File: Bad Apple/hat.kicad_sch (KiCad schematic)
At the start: 6 parts, among them J1 GPIO, U1 CAT24C256

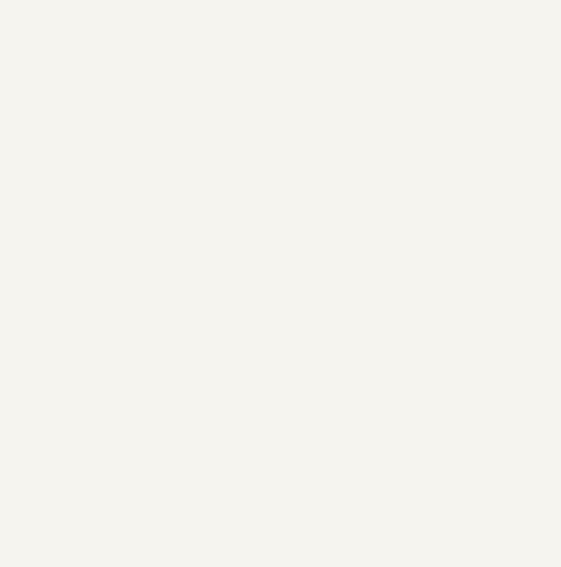
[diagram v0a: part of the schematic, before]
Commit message: chore(pcb): metadata stuff
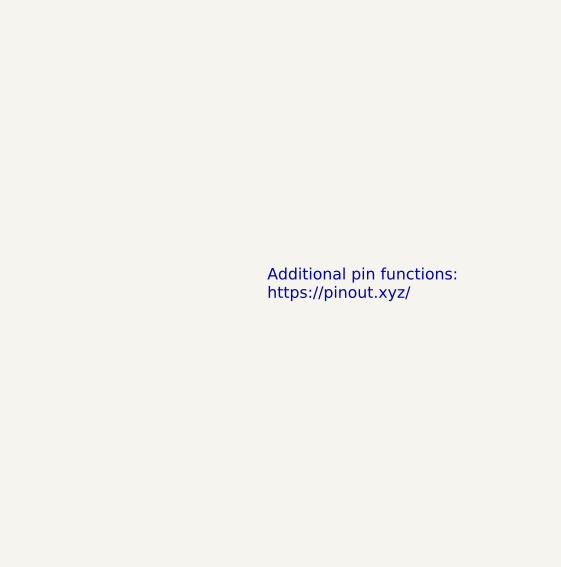
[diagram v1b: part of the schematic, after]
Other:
- note added: "Additional pin functions: https://pinout.xyz/"
- company: (none) -> Mixed Engineering Group 3 | STEM 12-Altruism / AY 2526 | CIT-U SHS
- title: (none) -> Autonomous  Courier Robot "Bad Apple"
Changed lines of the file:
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@@
 	(generator_version "9.0")
 	(paper "A4")
+	(title_block
+		(title "Autonomous  Courier Robot \"Bad Apple\"")
+		(date "2025-08-28")
+		(rev "1")
+		(company "Mixed Engineering Group 3 | STEM 12-Altruism / AY 2526 | CIT-U SHS")
+		(comment 4 "This sheet defines the Raspberry Pi HAT interface")
+	)
 	(text "ID_SD and ID_SC PINS:\nThese pins are reserved for HAT ID EEPROM.\n\nAt boot time this I2C interface will be\ninterrogated to look for an EEPROM\nthat identifes the attached board and\nallows automagic setup of the GPIOs\n(and optionally, Linux drivers).\n\nBridging JP1 enables write protection.\n\nDO NOT USE these pins for anything other\nthan attaching an I2C ID EEPROM. Leave\nunconnected if ID EEPROM not required."
 		(exclude_from_sim no)
@@
 		(effects
 			(font
+				(size 1.27 1.27)
+			)
+			(justify left bottom)
+		)
+	)
+	(text "Additional pin functions:\nhttps://pinout.xyz/"
+		(exclude_from_sim no)
+		(at 176.53 165.1 0)
+		(effects
+			(font

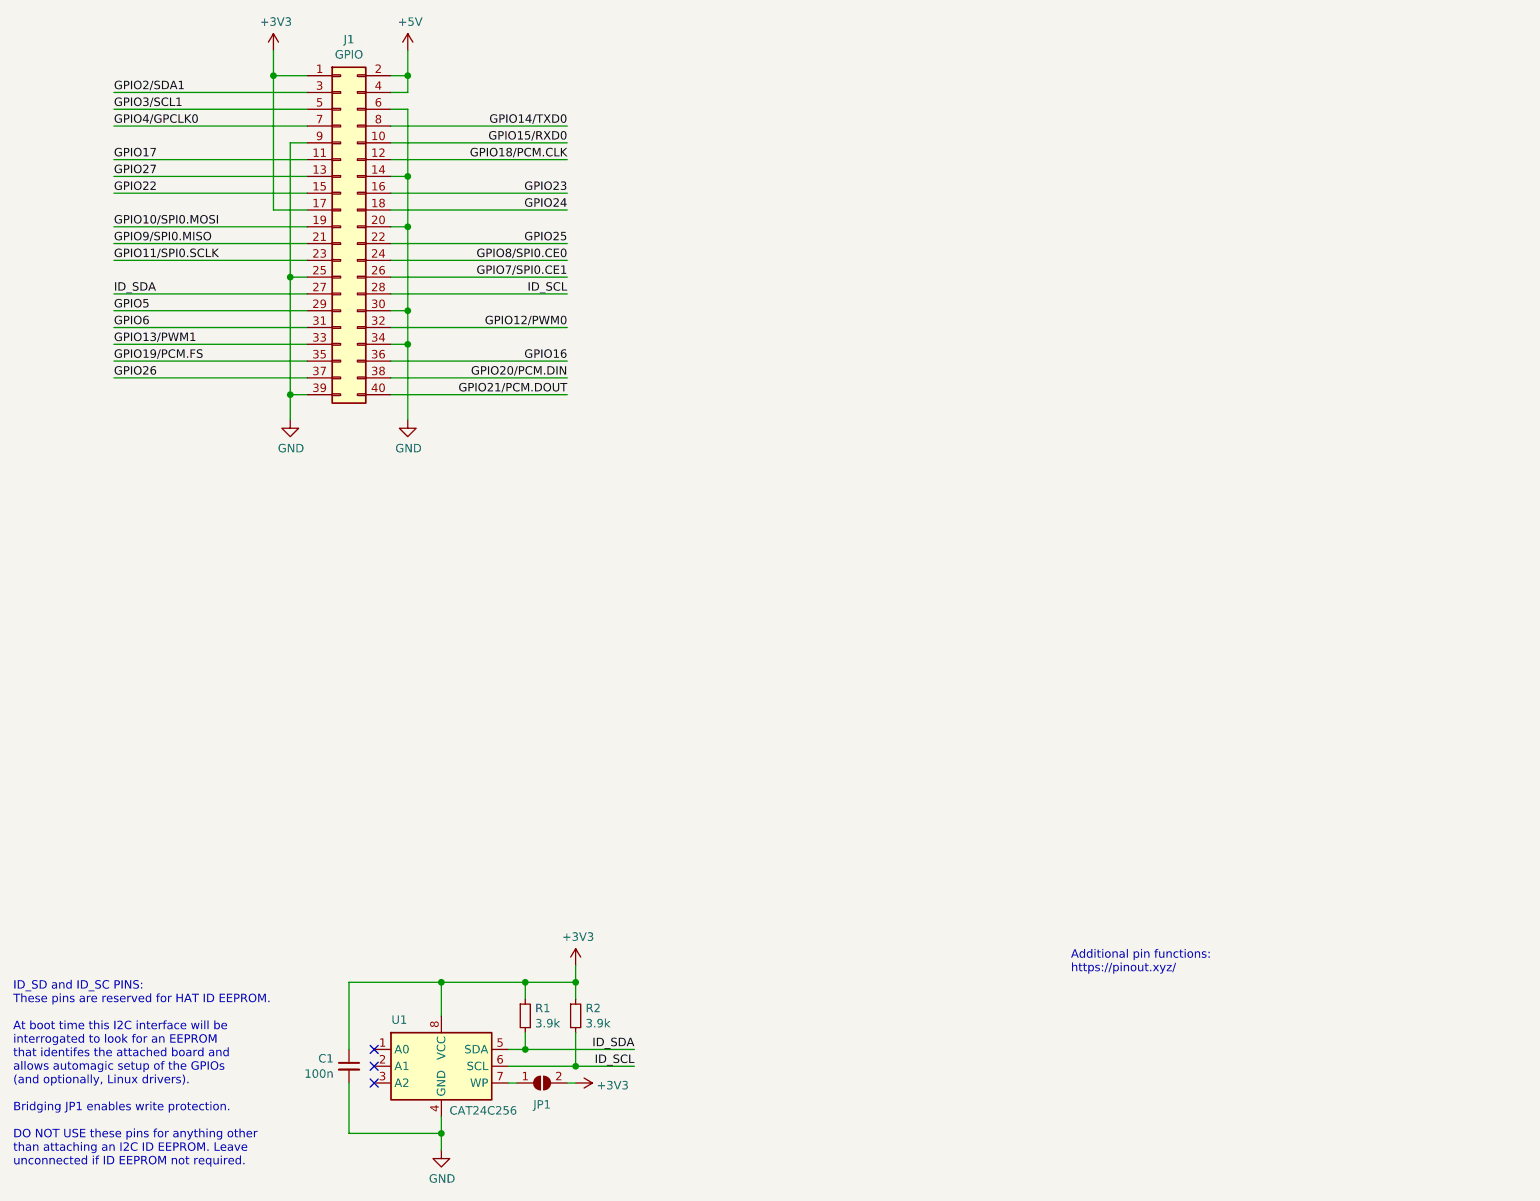
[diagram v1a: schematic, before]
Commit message: feat(pcb): motor subsystem
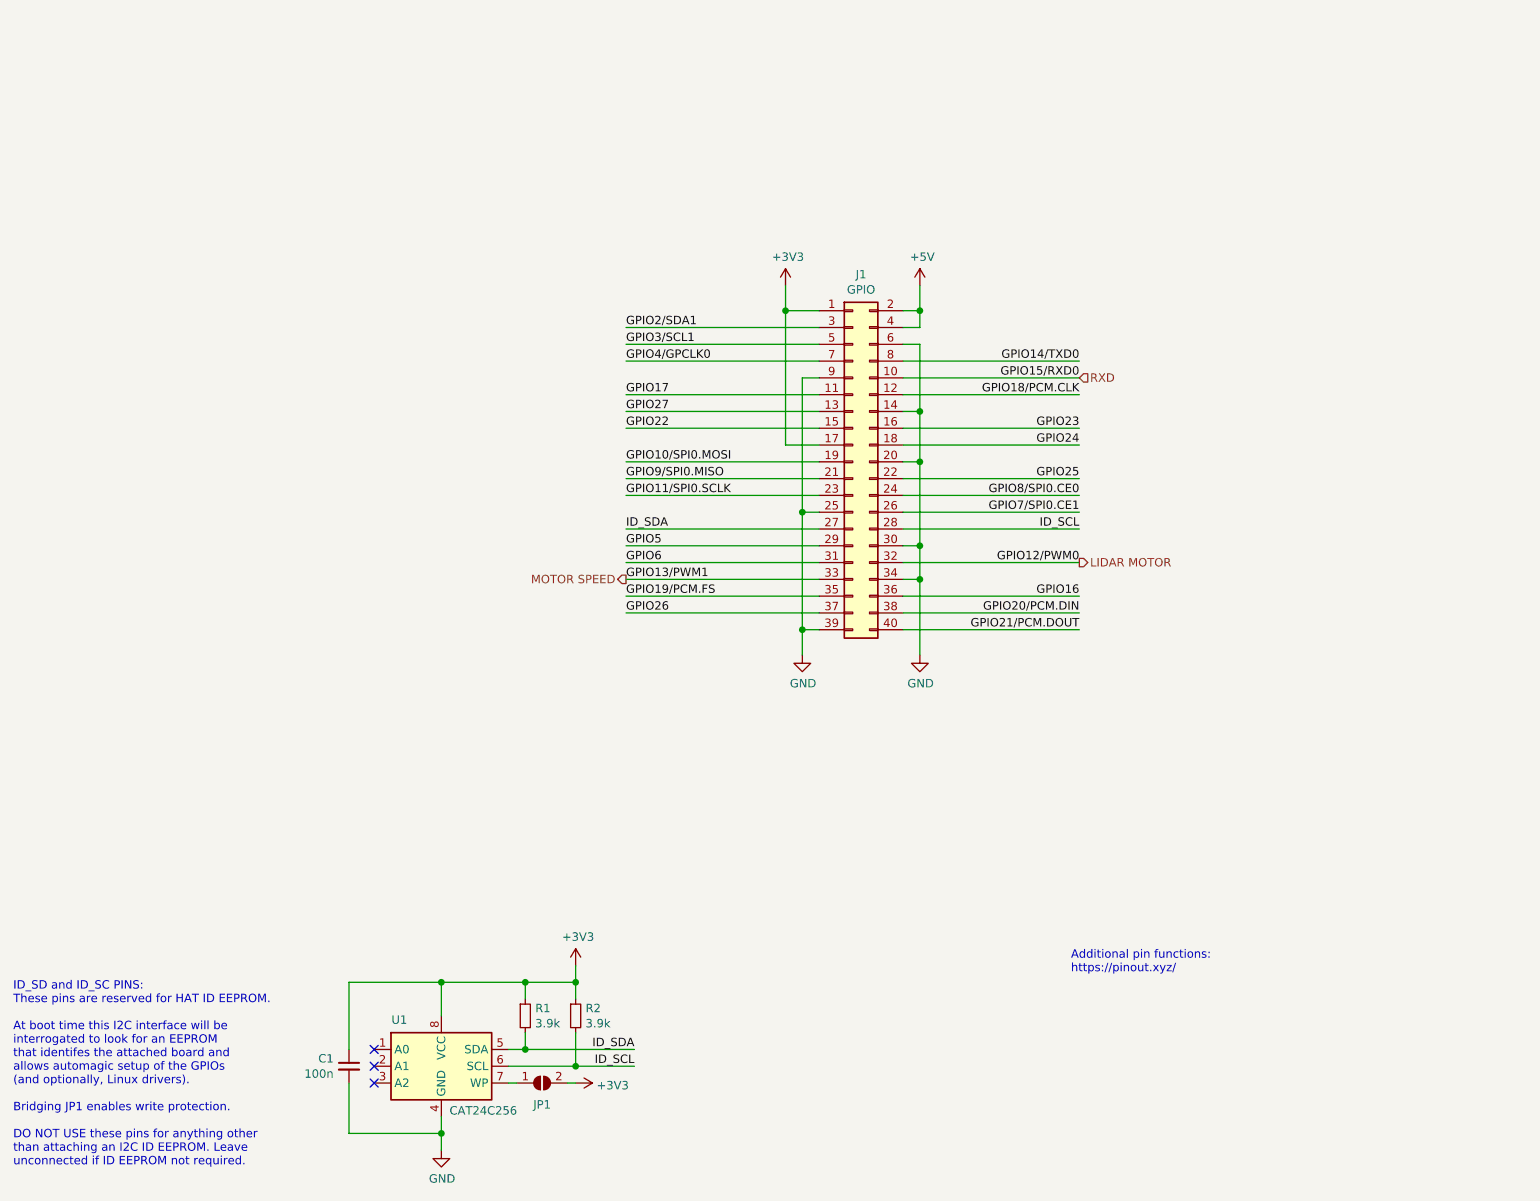
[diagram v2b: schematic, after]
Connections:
- net GPIO12/PWM0 renamed LIDAR MOTOR
- net GPIO13/PWM1 renamed MOTOR SPEED
- net GPIO15/RXD0 renamed RXD
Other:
- moved on the sheet: J1

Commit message: feat(pcb): connections n stuff
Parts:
- added J8: Conn_01x02, symbol Connector_Generic:Conn_01x02
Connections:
- net ID_SCL: now also J8.1 (Pin_1)
- net ID_SDA: now also J8.2 (Pin_2)
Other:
- note added: "I^{2}C Interface for the Identification EEPROM. Only used during development to flash said EEPROM with information required for ease of use"
- note added: "Raspberry Pi GPIO Pinout"
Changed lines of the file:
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@@
 		(comment 4 "This sheet defines the Raspberry Pi HAT interface")
+	)
+	(text "Raspberry Pi GPIO Pinout"
+		(exclude_from_sim no)
+		(at 196.596 60.452 0)
+		(effects
+			(font
+				(size 1.27 1.27)
+			)
+		)
+	)
+	(text "I^{2}C Interface for the Identification\nEEPROM. Only used during development to\nflash said EEPROM with information required\nfor ease of use"
+		(exclude_from_sim no)
+		(at 48.514 141.478 0)
+		(effects
+			(font
+				(size 1.27 1.27)
+			)
+			(justify left)
+		)
 	)
 	(text "ID_SD and ID_SC PINS:\nThese pins are reserved for HAT ID EEPROM.\n\nAt boot time this I2C interface will be\ninterrogated to look for an EEPROM\nthat identifes the attached board and\nallows automagic setup of the GPIOs\n(and optionally, Linux drivers).\n\nBridging JP1 enables write protection.\n\nDO NOT USE these pins for anything other\nthan attaching an I2C ID EEPROM. Leave\nunconnected if ID EEPROM not required."
@@
 	(wire
 		(pts
+			(xy 25.4 138.43) (xy 39.37 138.43)
+		)
+		(stroke
+			(width 0)
+			(type default)
+		)
+	)
+	(wire
+		(pts
 			(xy 138.43 67.31) (xy 109.22 67.31)
 		)
@@
 			(width 0)
 			(type solid)
+		)
+	)
+	(wire
+		(pts
+			(xy 25.4 140.97) (xy 39.37 140.97)
+		)
+		(stroke
+			(width 0)
+			(type default)
 		)
 	)
@@
 		)
 	)
+	(label "ID_SCL"
+		(at 25.4 140.97 180)
+		(effects
+			(font
+				(size 1.27 1.27)
+			)
+			(justify right bottom)
+		)
+	)
 	(label "GPIO9{slash}SPI0.MISO"
 		(at 109.22 90.17 0)
@@
 	(label "GPIO14{slash}TXD0"
 		(at 177.8 72.39 180)
+		(effects
+			(font
+				(size 1.27 1.27)
+			)
+			(justify right bottom)
+		)
+	)
+	(label "ID_SDA"
+		(at 25.4 138.43 180)
 		(effects
 			(font
@@
 					(unit 1)
 				)
+			)
+		)
+	)
+	(symbol
+		(lib_id "Connector_Generic:Conn_01x02")
+		(at 44.45 140.97 0)
+		(mirror x)
+		(unit 1)
+		(exclude_from_sim no)
+		(in_bom yes)
+		(on_board yes)
+		(dnp no)
+		(property "Reference" "J8"
+			(at 44.45 132.08 0)
+			(effects
+				(font
+					(size 1.27 1.27)
+				)
+			)
+		)
+		(property "Value" "Conn_01x02"
+			(at 44.45 134.62 0)
+			(effects
+				(font
+					(size 1.27 1.27)
+				)
+			)
+		)
+		(property "Footprint" ""
+			(at 44.45 140.97 0)
+			(effects
+				(font
+					(size 1.27 1.27)
+				)
+				(hide yes)
+			)
+		)
+		(property "Datasheet" "~"
+			(at 44.45 140.97 0)
+			(effects
+				(font
+					(size 1.27 1.27)
+				)
+				(hide yes)
+			)
+		)
+		(property "Description" "Generic connector, single row, 01x02, script generated (kicad-library-utils/schlib/autogen/connector/)"
+			(at 44.45 140.97 0)
+			(effects
+				(font
+					(size 1.27 1.27)
+				)
+				(hide yes)
+			)
+		)
+		(pin "1"
+		)
+		(pin "2"
+		)
+		(instances
+			(project ""
+				(path "/e63e39d7-6ac0-4ffd-8aa3-1841a4541b55/b30abb3a-5689-47ca-b698-70986eaac049"
+					(reference "J8")
+					(unit 1)
+				)

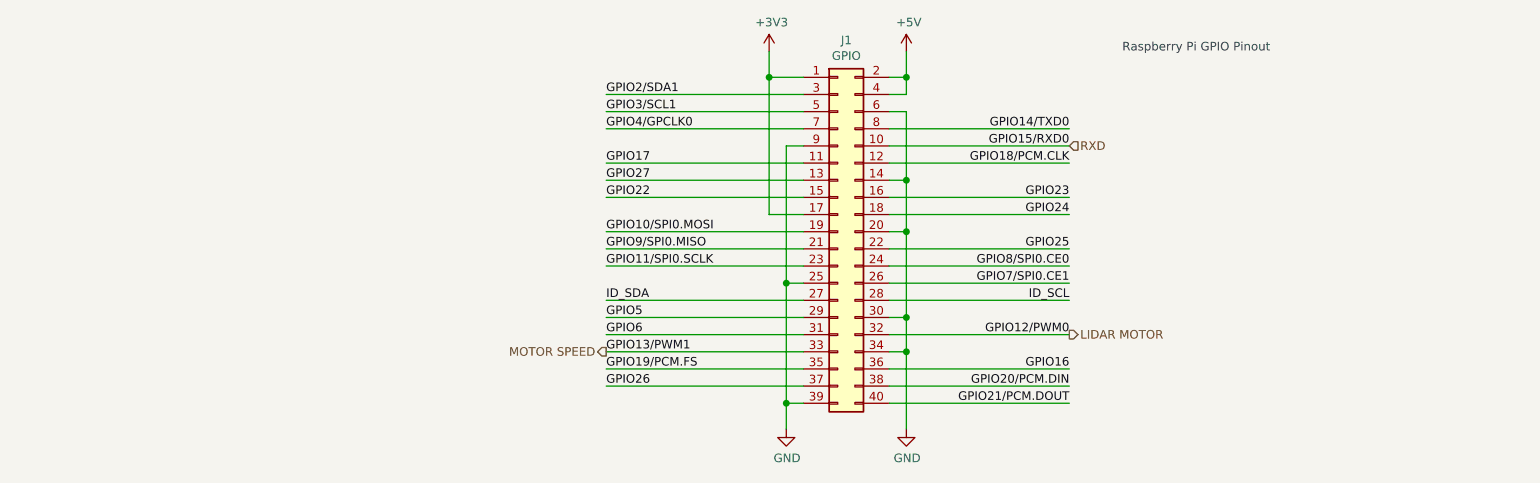
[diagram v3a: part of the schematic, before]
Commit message: feat(pcb):  connected everything to the HAT doc(pcb):  Added descriptions to the J1 pinout
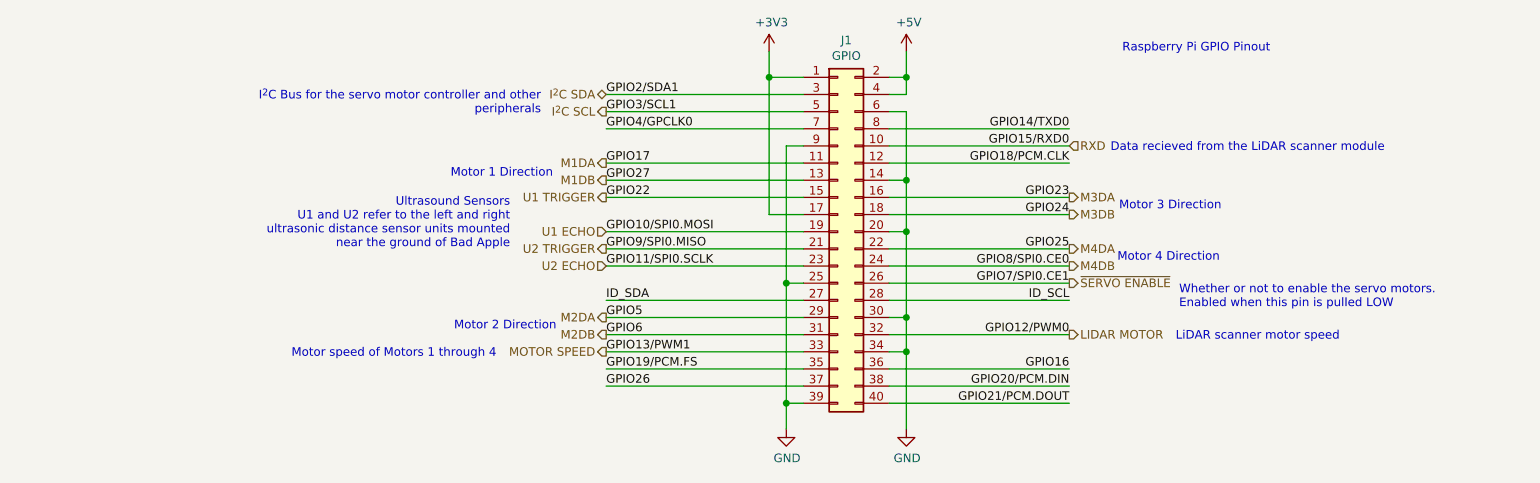
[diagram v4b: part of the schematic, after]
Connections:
- net GPIO10/SPI0.MOSI renamed U1 ECHO
- net GPIO11/SPI0.SCLK renamed U2 ECHO
- net GPIO17 renamed M1DA
- net GPIO22 renamed U1 TRIGGER
- net GPIO23 renamed M3DA
- net GPIO24 renamed M3DB
- net GPIO25 renamed M4DA
- net GPIO27 renamed M1DB
- net GPIO2/SDA1 renamed I^{2}C SDA
- net GPIO3/SCL1 renamed I^{2}C SCL
- net GPIO5 renamed M2DA
- net GPIO6 renamed M2DB
- net GPIO7/SPI0.CE1 renamed ~{SERVO ENABLE}
- net GPIO8/SPI0.CE0 renamed M4DB
- net GPIO9/SPI0.MISO renamed U2 TRIGGER
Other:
- note added: "Data recieved from the LiDAR scanner module"
- note added: "I^{2}C Bus for the servo motor controller and other peripherals"
- note added: "LiDAR scanner motor speed"
- note added: "Motor 1 Direction"
- note added: "Motor 2 Direction"
- note added: "Motor 3 Direction"
- note added: "Motor 4 Direction"
- note added: "Motor speed of Motors 1 through 4"
- note added: "Ultrasound Sensors U1 and U2 refer to the left and right ultrasonic distance sensor units mounted near the ground of Bad Apple"
- note added: "Whether or not to enable the servo motors. Enabled when this pin is pulled LOW"
